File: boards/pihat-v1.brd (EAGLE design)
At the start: 57.1 x 54 mm, 53 parts, among them J10 RASPBERRYPI-40-PIN-GPIO_PTH_N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, Q1 BSS138, Q13 BSS138, Q2 BSS138, Q3 BSS138

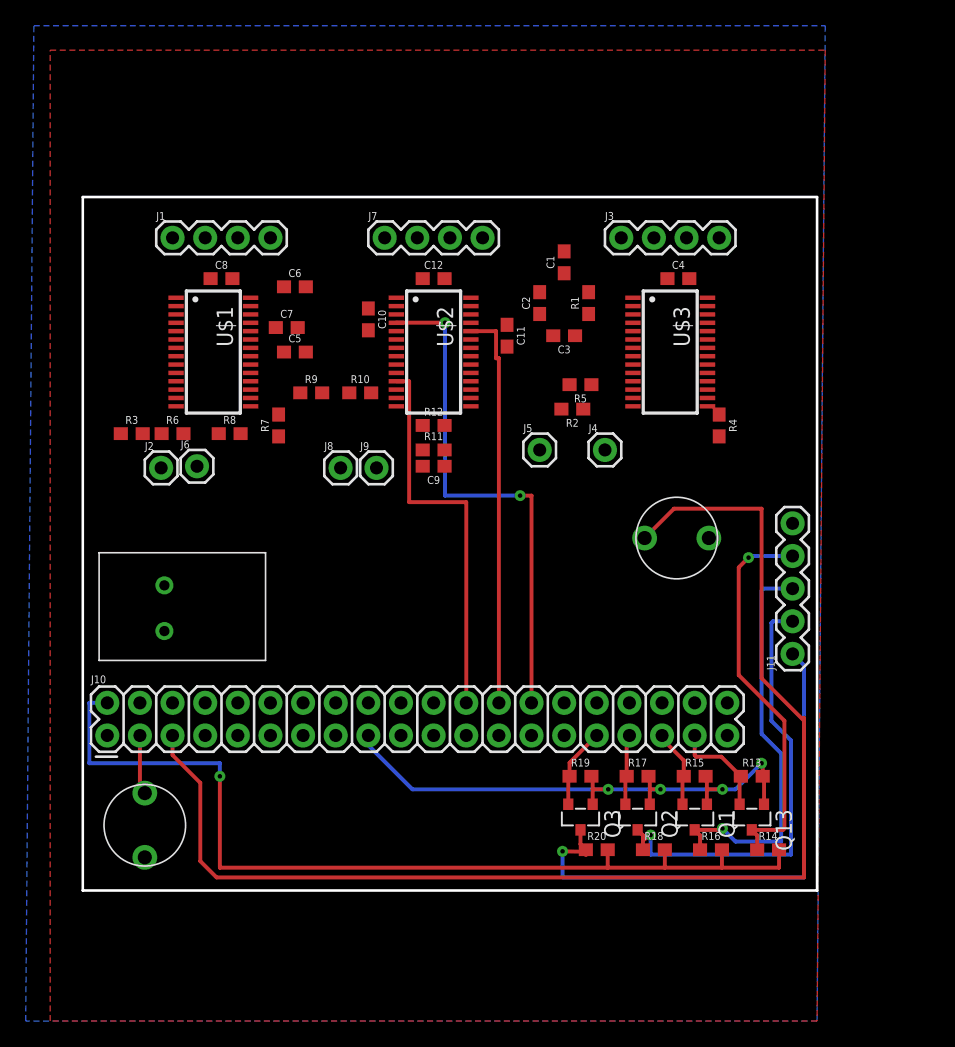
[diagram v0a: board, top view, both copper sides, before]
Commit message: pihat streamlined, largely laid out
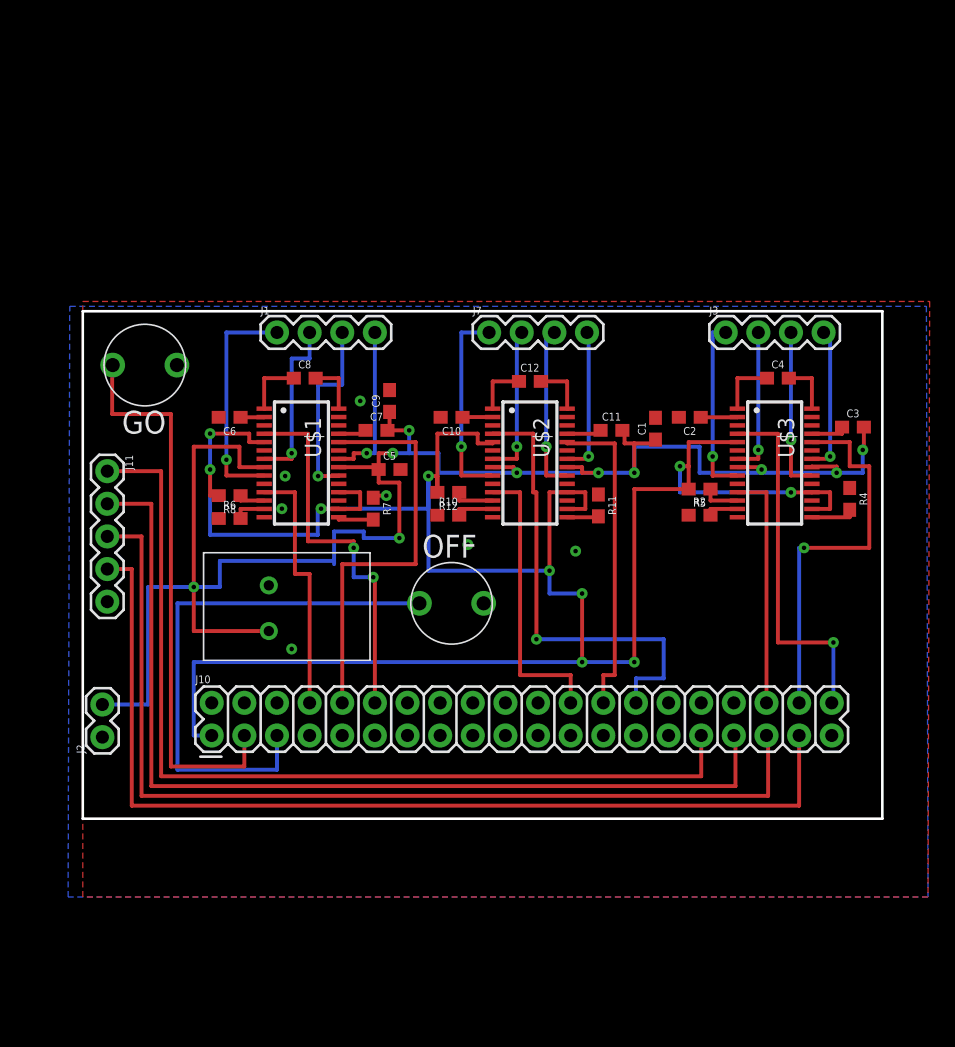
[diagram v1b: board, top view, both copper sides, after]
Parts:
- removed J4, J5, J6, J8, J9: (no value), SparkFun-Connectors:1X01
- removed Q1, Q13, Q2, Q3: BSS138, bss138_10:SOT23
- removed R1, R3, R9: 24.9k, SparkFun-Resistors:0603
- removed R13, R14, R15, R16, R17, R18, R19, R20: 10k, SparkFun-Resistors:0603
- J2: device SparkFun-Connectors:1X01 -> SparkFun-Connectors:1X02
- R10, R2, R6: value 50k -> 75k
- moved J11 55.2 mm to (1.91, 32.6), turned to 270 degrees
- moved U$4 35.8 mm to (4.83, 40.9), turned to 0 degrees
- moved C3 23.6 mm to (59.9, 36.1), turned to 0 degrees
- moved J2 21.4 mm to (1.52, 11.9), turned to 90 degrees
- moved U$5 18.2 mm to (28.7, 22.4)
- moved C1 14.8 mm to (44.6, 35.9)
- moved C2 14.7 mm to (47.2, 36.8), turned to 180 degrees
- moved R11 13.5 mm to (40.1, 30.0), turned to 270 degrees
- moved R2 12.9 mm to (48.0, 29.2), turned to 0 degrees
- moved R5 12.3 mm to (48.0, 31.2)
- moved U$3 11.9 mm to (53.8, 33.3)
- moved C5 11.7 mm to (23.9, 32.8)
- moved R10 11.7 mm to (28.4, 29.2)
- moved R4 11.7 mm to (59.7, 30.5)
- moved U$2 11.4 mm to (34.8, 33.3)
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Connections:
- removed net N$26: J4.1, R1.2, R2.1
- removed net N$31: J2.1, R3.2, R6.1
- removed net N$48: J8.1, R10.1, R9.2
- removed net N$53: J11.1, Q3.3, R20.1
- removed net N$54: J11.2, Q2.3, R18.1
- removed net N$55: J11.3, Q1.3, R16.1
- removed net N$56: J11.4, Q13.3, R14.1
- net 12V: now also J2.2
- net 3.3V: no longer Q1.1, Q13.1, Q2.1, Q3.1, R13.2, R15.2, R17.2, R19.2
- net 5V: no longer R14.2, R16.2, R18.2, R20.2
- net CONTROL1: now also J11.1; no longer Q3.2, R19.1
- net CONTROL2: now also J11.2; no longer Q2.2, R17.1
- net CONTROL3: now also J11.3; no longer Q1.2, R15.1
- net CONTROL4: now also J11.4; no longer Q13.2, R13.1
- net GND: now also J2.1, R10.1, R2.1, R6.1; no longer R1.1, R3.1, R9.1
- net N$24: no longer J5.1
- net N$29: no longer J6.1
- net N$47: no longer J9.1
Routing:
- net 12V: track 0.00 -> 143.9 mm, vias 0 -> 10
- net 3.3V: track 46.8 -> 176.5 mm, vias 4 -> 10
- net 5V: track 73.5 -> 0.00 mm, vias 1 -> 0
- net CONTROL3: track 6.09 -> 76.5 mm
- net CONTROL4: track 8.02 -> 77.7 mm
- net CONTROL2: track 5.48 -> 74.9 mm
- net CONTROL1: track 6.27 -> 73.2 mm
- net OFF-GPIO3: track 98.6 -> 42.2 mm
- net N$53: track 43.1 -> 0.00 mm, vias 1 -> 0
- net GO-GPIO2: track 4.64 -> 44.0 mm
- net N$54: track 35.3 -> 0.00 mm, vias 1 -> 0
- net STEP3: track 0.00 -> 32.0 mm
- net N$55: track 31.6 -> 0.00 mm, vias 1 -> 0
- net N$56: track 30.7 -> 0.00 mm, vias 1 -> 0
- net STEP1: track 0.00 -> 30.3 mm, vias 0 -> 1
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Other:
- board size 57.1 x 54 mm -> 62.2 x 39.5 mm
- board text added: "GO"
- board text added: "OFF"
